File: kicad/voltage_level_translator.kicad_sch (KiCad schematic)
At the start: 16 parts, among them Q1 2N7002, Q2 2N7002, Q3 2N7002, U3 TMUX1574PW, U7 TMUX1574PW, U8 TXS0108EPW, U9 TXS0108EPW

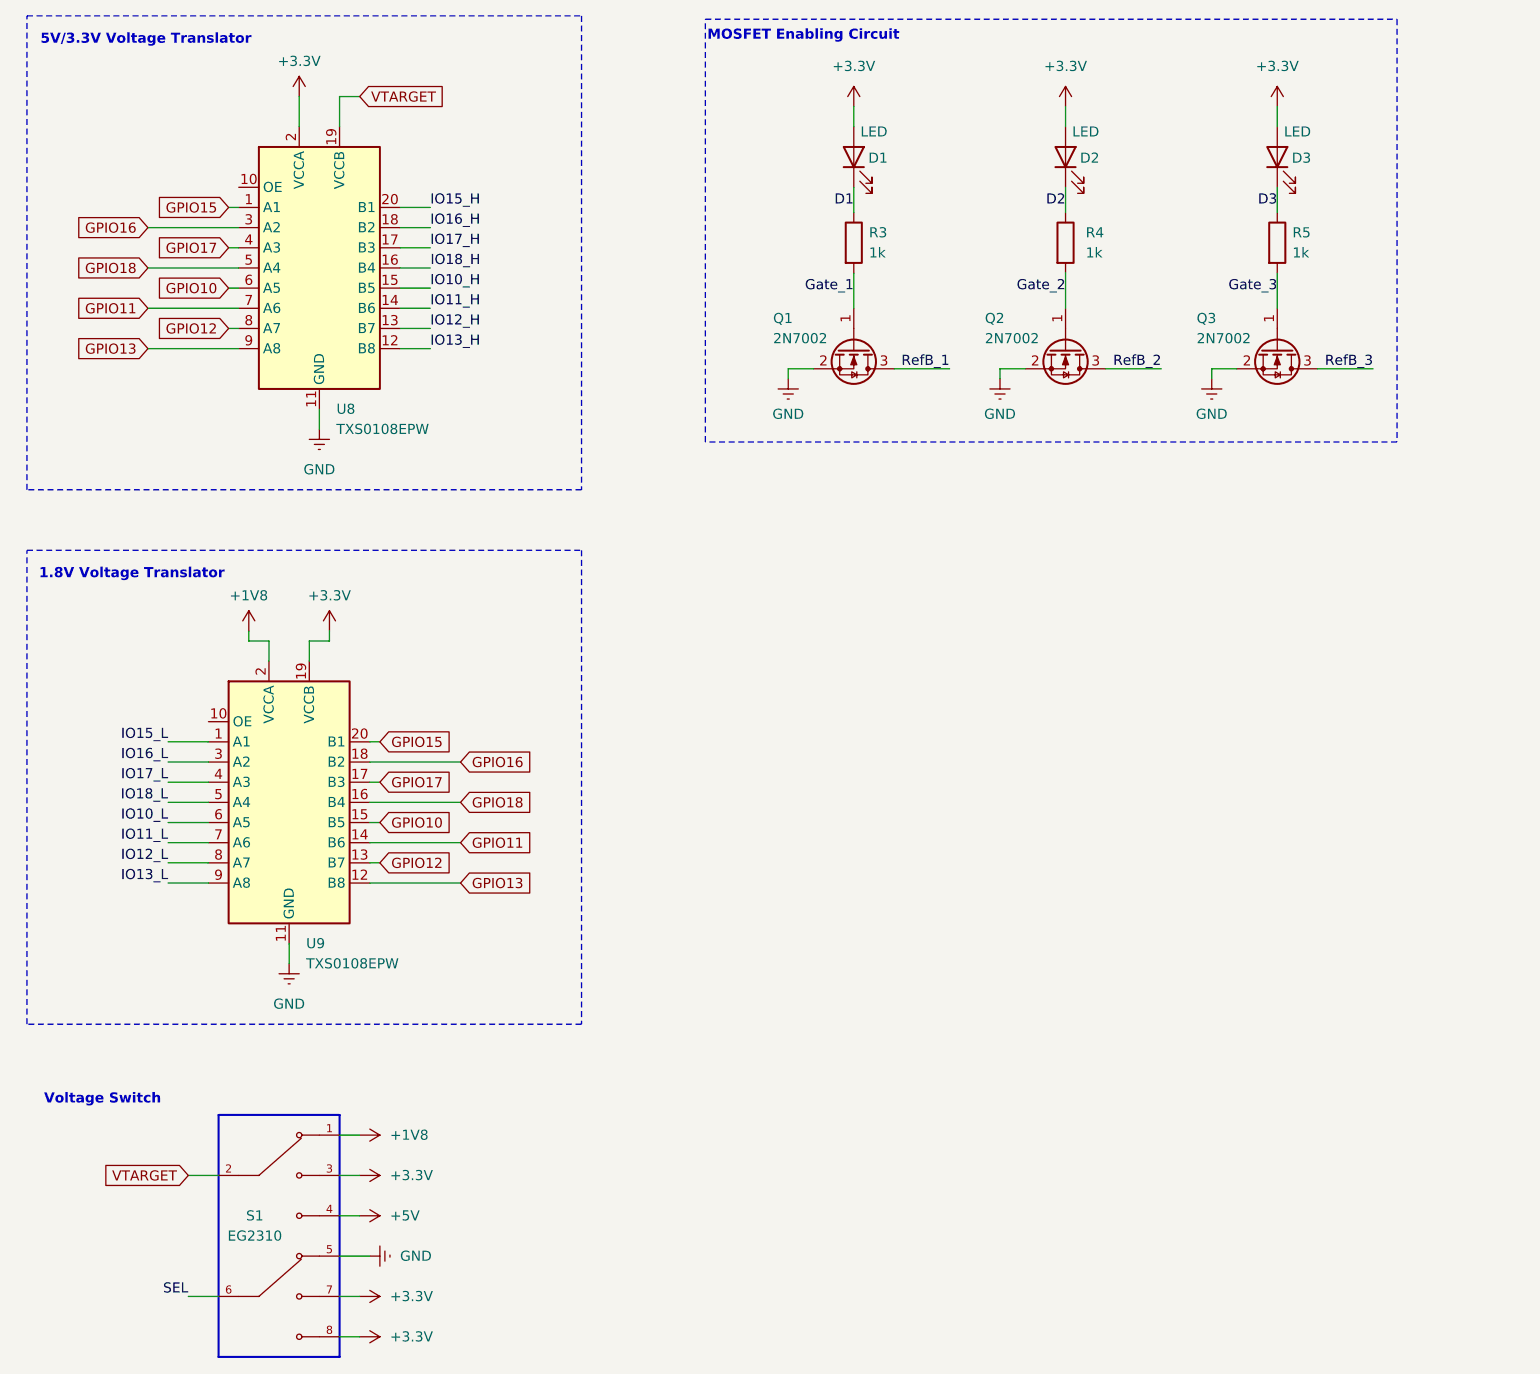
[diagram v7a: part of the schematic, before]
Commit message: Eliminated old traces
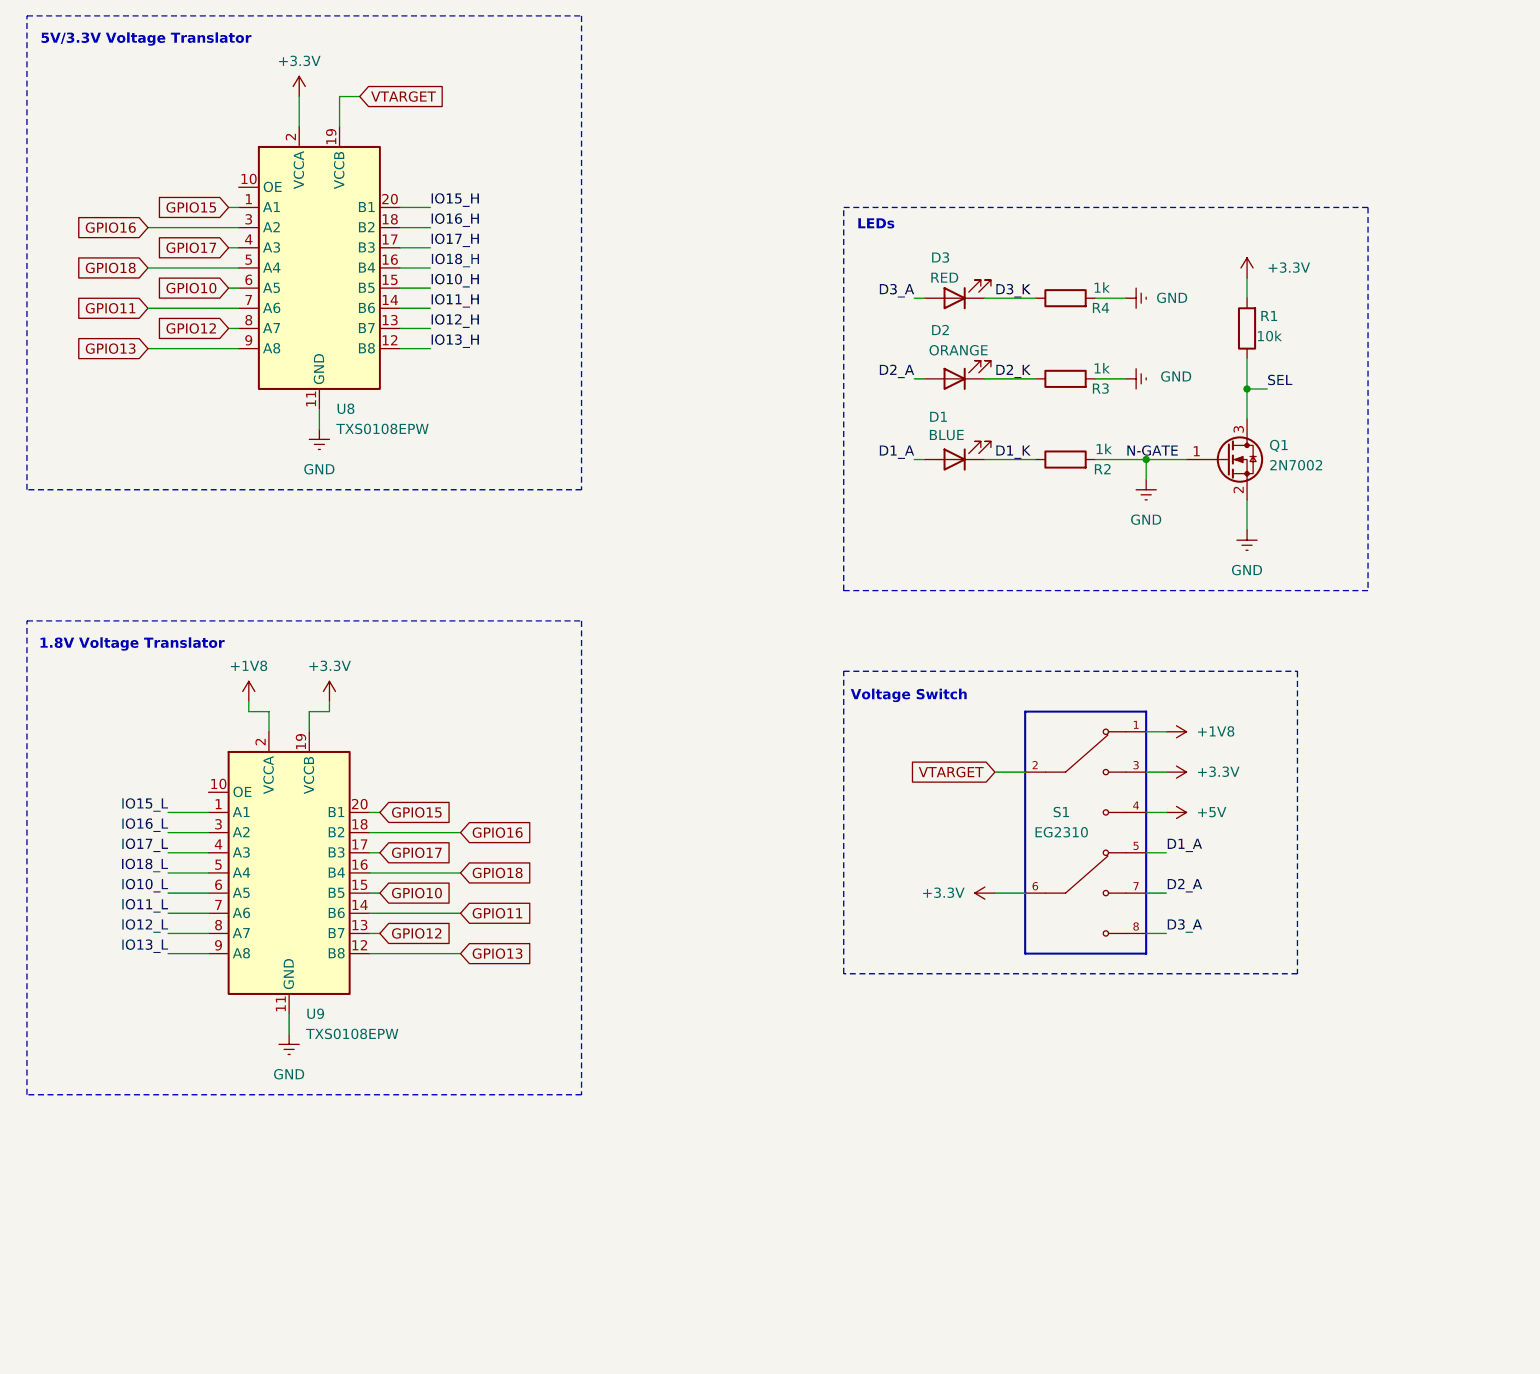
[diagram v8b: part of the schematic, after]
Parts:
- removed Q2, Q3: 2N7002, Package_TO_SOT_SMD:SOT-23, symbol Transistor_FET:2N7002
- added R1: 10k, Resistor_SMD:R_0805_2012Metric, symbol Device:R
- D1: value LED -> BLUE
- D2: renamed from D3; value LED -> ORANGE
- D3: renamed from D2; value LED -> RED
- renumbered R3 to R2, R5 to R3
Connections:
- net Gate_1 is gone; now on net GND: Q1.1 (G), R2.2
- net Gate_2 is gone; now on net GND: R4.2
- net Gate_3 is gone; now on net GND: R3.2
- net RefB_1 is gone; now on net SEL: Q1.3 (D)
- net +3.3V: now also S1.6, R1.2; no longer D1.2 (A), D2.2 (A), D3.2 (A), S1.7, S1.8
- net GND: no longer S1.5
- net SEL: now also R1.1; no longer S1.6
- net D1 renamed D1_K
- net D2 renamed D3_K
- net D3 renamed D2_K
- new net D1_A: D1.2 (A), S1.5
- new net D2_A: D2.2 (A), S1.7
- new net D3_A: D3.2 (A), S1.8
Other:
- note added: "LEDs"
- note removed: "MOSFET Enabling Circuit"
- moved on the sheet: D1, D2, D3, Q1, R2, R3, R4, S1, U9
